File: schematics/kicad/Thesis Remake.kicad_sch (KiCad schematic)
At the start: 106 parts, among them J1 SJ2-35853B-SMT-TR, J2 Conn_01x18, J3 Conn_01x18, J4 Conn_01x01_Pin, J5 Conn_01x01_Pin, J6 Conn_01x01_Pin, J7 Conn_01x01_Pin, Q1 MMBT7002K, U10 MCP6001-OT, U11 MCP6001-OT, U2 PCM5102, U3 SN74LVC1G3157, U5 RT9080-33GJ5, U6 LM2940CT-5.0_MOD, U7 TPA711, U8 LM2940CT-5.0_MOD, U9 MCP6001-OT

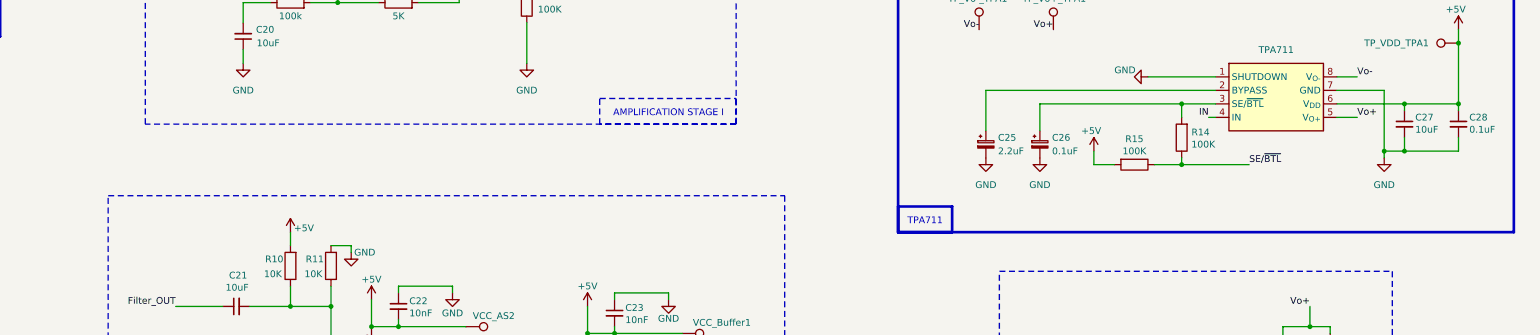
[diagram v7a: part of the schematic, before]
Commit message: Bluetooth works. Waveform generation works.
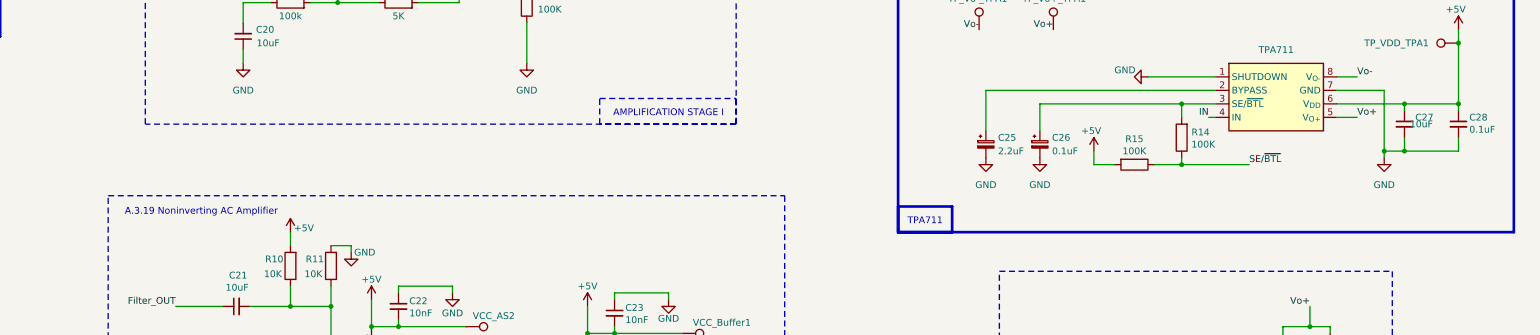
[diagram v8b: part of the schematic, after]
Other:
- note added: "A.3.19 Noninverting AC Amplifier"
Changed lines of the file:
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@@
 				(size 1.27 1.27)
 			)
+			(href "https://www.mouser.de/ProductDetail/Texas-Instruments/LM2940CT-5.0?qs=X1J7HmVL2ZHPtClZnI0H9A%3D%3D&srsltid=AfmBOooXmYCn6kktzCuK6TYLYlqacIcQRMEHhtZtGWFUuRpZVCvzZQb-")
 		)
 	)
@@
 				(size 1.27 1.27)
 			)
+			(href "https://www.mouser.de/ProductDetail/Texas-Instruments/LM2940CT-5.0?qs=X1J7HmVL2ZHPtClZnI0H9A%3D%3D&srsltid=AfmBOooXmYCn6kktzCuK6TYLYlqacIcQRMEHhtZtGWFUuRpZVCvzZQb-")
 		)
 	)
@@
 		)
 	)
+	(text "A.3.19 Noninverting AC Amplifier"
+		(exclude_from_sim no)
+		(at 309.626 120.65 0)
+		(effects
+			(font
+				(size 1.27 1.27)
+			)
+		)
+	)
 	(text "JACK OUTPUT"
 		(exclude_from_sim no)
@@
 				(size 1.27 1.27)
 			)
+			(href "https://www.mouser.de/ProductDetail/Richtek/RT9080-33GJ5?qs=amGC7iS6iy9hJG6yuLjyPQ%3D%3D")
 		)
 	)
@@
 			"AAAAAAAAAAAAAAAAAAAAAAAAAAAAAAAAAAAAAAAAAAAAAAAAAAAAAAAAAAAAAAAAAAAAAAAAAAAA"
 			"AAAAAAAAAAAAAAAAAAAAAAAAAAAAAAAAAAAAAAAAAAAAAAAAAAAAAAAAAAAAAAAAAAAAAAAAAAAA"
+			"AAAAAAAAAAAAAAAAAAAAAAAAAAAAAAAAAAAAAAAAAAAAAAAAAAAAAAAAAAAAAAAAAAAAAAAAAAAA"
+			"AAAAAAAAAAAAAAAAAAAAAAAAAAAAAAAAAAAAAAAAAAAAAAAAAAAAAAAAAAAAAAAAAAAAAAAAAAAA"
+			"AAAAAAAAAAAAAAAAAAAAAAAAAAAAAAAAAAAAAAAAAAAAAAAAAAAAAAAAAAAAAAAAAAAAAAAAAAAA"
+			"AAAAAAAAAAAAAAAAAAAAAAAAAAAAAAAAAAAAAAAAAAAAAAAAAAAAAAAAAAAAAAAAAAAAAAAAAAAA"
+			"AAAAAAAAAAAAAAAAAAAAAAAAAAAAAAAAAAAAAAAAAAAAAAAAAAAAAAAAAAAAAAAAAAAAAAAAAAAA"
+			"AAAAAAAAAAAAAAAAAAAAAAAAAAAAAAAAAAAAAAAAAAAAAAAAAAAAAAAAAAAAAAAAAAAAAAAAAAAA"
+			"AAAAAAAAAAAAAAAAAAAAAAAAAAAAAAAAAAAAAAAAAAAAAAAAAAAAAAAAAAAAAAAAAAAAAAAAAAAA"
+			"AAAAAAAAAAAAAAAAAAAAAAAAAAAAAAAAAAAAAAAAAAAAAAAAAAAAAAAAAAAAAAAAAAAAAAAAAAAA"
+			"AAAAAAAAAAAAAAAAAAAAAAAAAAAAAAAAAAAAAAAAAAAAAAAAAAAAAAAAAAAAAAAAAAAAAAAAAAAA"
+			"AAAAAAAAAAAAAAAAAAAAAAAAAAAAAAAAAAAAAAAAAAAAAAAAAAAAAAAAAAAAAAAAAAAAAAAAAAAA"
+			"AAAAAAAAAAAAAAAAAAAAAAAAAAAAAAAAAAAAAAAAAAAAAAAAAAAAAAAAAAAAAAAAAAAAAAAAAAAA"
+			"AAAAAAAAAAAAAAAAAAAAAAAAAAAAAAAAAAAAAAAAAAAAAAAAAAAAAAAAAAAAAAAAAAAAAAAAAAAA"
+			"AAAAAAAAAAAAAAAAAAAAAAAAAAAAAAAAAAAAAAAAAAAAAAAAAAAAAAAAAAAAAAAAAAAAAAAAAAAA"
+			"AAAAAAAAAAAAAAAAAAAAAAAAAAAAAAAAAAAAAAAAAAAAAAAAAAAAAAAAAAAAAAAAAAAAAAAAAAAA"
+			"AAAAAAAAAAAAAAAAAAAAAAAAAAAAAAAAAAAAAAAAAAAAAAAAAAAAAAAAAAAAAAAAAAAAAAAAAAAA"
+			"AAAAAAAAAAAAAAAAAAAAAAAAAAAAAAAAAAAAAAAAAAAAAAAAAAAAAAAAAAAAAAAAAAAAAAAAAAAA"
+			"AAAAAAAAAAAAAAAAAAAAAAAAAAAAAAAAAAAAAAAAAAAAAAAAAAAAAAAAAAAAAAAAAAAAAAAAAAAA"
+			"AAAAAAAAAAAAAAAAAAAAAAAAAAAAAAAAAAAAAAAAAAAAAAAAAAAAAAAAAAAAAAAAAAAAAAAAAAAA"
+			"AAAAAAAAAAAAAAAAAAAAAAAAAAAAAAAAAAAAAAAAAAAAAAAAAAAAAAAAAAAAAAAAAAAAAAAAAAAA"
+			"AAAAAAAAAAAAAAAAAAAAAAAAAAAAAAAAAAAAAAAAAAAAAAAAAAAAAAAAAAAAAAAAAAAAAAAAAAAA"
+			"AAAAAAAAAAAAAAAAAAAAAAAAAAAAAAAAAAAAAAAAAAAAAAAAAAAAAAAAAAAAAAAAAAAAAAAAAAAA"
+			"AAAAAAAAAAAAAAAAAAAAAAAAAAAAAAAAAAAAAAAAAAAAAAAAAAAAAAAAAAAAAAAAAAAAAAAAAAAA"
+			"AAAAAAAAAAAAAAAAAAAAAAAAAAAAAAAAAAAAAAAAAAAAAAAAAAAAAAAAAAAAAAAAAAAAAAAAAAAA"
+			"AAAAAAAAAAAAAAAAAAAAAAAAAAAAAAAAAAAAAAAAAAAAAAAAAAAAAAAAAAAAAAAAAAAAAAAAAAAA"
+			"AAAAAAAAAAAAAAAAAAAAAAAAAAAAAAAAAAAAAAAAAAAAAAAAAAAAAAAAAAAAAAAAAAAAAAAAAAAA"
+			"AAAAAAAAAAAAAAAAAAAAAAAAAAAAAAAAAAAAAAAAAAAAAAAAAAAAAAAAAAAAAAAAAAAAAAAAAAAA"
+			"AAAAAAAAAAAAAAAAAAAAAAAAAAAAAAAAAAAAAAAAAAAAAAAAAAAAAAAAAAAAAAAAAAAAAAAAAAAA"
+			"AAAAAAAAAAAAAAAAAAAAAAAAAAAAAAAAAAAAAAAAAAAAAAAAAAAAAAAAAAAAAAAAAAAAAAAAAAAA"
+			"AAAAAAAAAAAAAAAAAAAAAAAAAAAAAAAAAAAAAAAAAAAAAAAAAAAAAAAAAAAAAAAAAAAAAAAAAAAA"
+			"AAAAAAAAAAAAAAAAAAAAAAAAAAAAAAAAAAAAAAAAAAAAAAAAAAAAAAAAAAAAAAAAAAAAAAAAAAAA"
+			"AAAAAAAAAAAAAAAAAAAAAAAAAAAAAAAAAAAAAAAAAAAAAAAAAAAAAAAAAAAAAAAAAAAAAAAAAAAA"
+			"AAAAAAAAAAAAAAAAAAAAAAAAAAAAAAAAAAAAAAAAAAAAAAAAAAAAAAAAAAAAAAAAAAAAAAAAAAAA"
+			"AAAAAAAAAAAAAAAAAAAAAAAAAAAAAAAAAAAAAAAAAAAAAAAAAAAAAAAAAAAAAAAAAAAAAAAAAAAA"
+			"AAAAAAAAAAAAAAAAAAAAAAAAAAAAAAAAAAAAAAAAAAAAAAAAAAAAAAAAAAAAAAAAAAAAAAAAAAAA"
+			"AAAAAAAAAAAAAAAAAAAAAAAAAAAAAAAAAAAAAAAAAAAAAAAAAAAAAAAAAAAAAAAAAAAAAAAAAAAA"
+			"AAAAAAAAAAAAAAAAAAAAAAAAAAAAAAAAAAAAAAAAAAAAAAAAAAAAAAAAAAAAAAAAAAAAAAAAAAAA"
+			"AAAAAAAAAAAAAAAAAAAAAAAAAAAAAAAAAAAAAAAAAAAAAAAAAAAAAAAAAAAAAAAAAAAAAAAAAAAA"
+			"AAAAAAAAAAAAAAAAAAAAAAAAAAAAAAAAAAAAAAAAAAAAAAAAAAAAAAAAAAAAAAAAAAAAAAAAAAAA"
+			"AAAAAAAAAAAAAAAAAAAAAAAAAAAAAAAAAAAAAAAAAAAAAAAAAAAAAAAAAAAAAAAAAAAAAAAAAAAA"
+			"AAAAAAAAAAAAAAAAAAAAAAAAAAAAAAAAAAAAAAAAAAAAAAAAAAAAAAAAAAAAAAAAAAAAAAAAAAAA"
+			"AAAAAAAAAAAAAAAAAAAAAAAAAAAAAAAAAAAAAAAAAAAAAAAAAAAAAAAAAAAAAAAAAAAAAAAAAAAA"
+			"AAAAAAAAAAAAAAAAAAAAAAAAAAAAAAAAAAAAAAAAAAAAAAAAAAAAAAAAAAAAAAAAAAAAAAAAAAAA"
+			"AAAAAAAAAAAAAAAAAAAAAAAAAAAAAAAAAAAAAAAAAAAAAAAAAAAAAAAAAAAAAAAAAAAAAAAAAAAA"
+			"AAAAAAAAAAAAAAAAAAAAAAAAAAAAAAAAAAAAAAAAAAAAAAAAAAAAAAAAAAAAAAAAAAAAAAAAAAAA"
+			"AAAAAAAAAAAAAAAAAAAAAAAAAAAAAAAAAAAAAAAAAAAAAAAAAAAAAAAAAAAAAAAAAAAAAAAAAAAA"
+			"AAAAAAAAAAAAAAAAAAAAAAAAAAAAAAAAAAAAAAAAAAAAAAAAAAAAAAAAAAAAAAAAAAAAAAAAAAAA"
+			"AAAAAAAAAAAAAAAAAAAAAAAAAAAAAAAAAAAAAAAAAAAAAAAAAAAAAAAAAAAAAAAAAAAAAAAAAAAA"
+			"AAAAAAAAAAAAAAAAAAAAAAAAAAAAAAAAAAAAAAAAAAAAAAAAAAAAAAAAAAAAAAAAAAAAAAAAAAAA"
+			"AAAAAAAAAAAAAAAAAAAAAAAAAAAAAAAAAAAAAAAAAAAAAAAAAAAAAAAAAAAAAAAAAAAAAAAAAAAA"
+			"AAAAAAAAAAAAAAAAAAAAAAAAAAAAAAAAAAAAAAAAAAAAAAAAAAAAAAAAAAAAAAAAAAAAAAAAAAAA"
+			"AAAAAAAAAAAAAAAAAAAAAAAAAAAAAAAAAAAAAAAAAAAAAAAAAAAAAAAAAAAAAAAAAAAAAAAAAAAA"
+			"AAAAAAAAAAAAAAAAAAAAAAAAAAAAAAAAAAAAAAAAAAAAAAAAAAAAAAAAAAAAAAAAAAAAAAAAAAAA"
+			"AAAAAAAAAAAAAAAAAAAAAAAAAAAAAAAAAAAAAAAAAAAAAAAAAAAAAAAAAAAAAAAAAAAAAAAAAAAA"
+			"AAAAAAAAAAAAAAAAAAAAAAAAAAAAAAAAAAAAAAAAAAAAAAAAAAAAAAAAAAAAAAAAAAAAAAAAAAAA"
+			"AAAAAAAAAAAAAAAAAAAAAAAAAAAAAAAAAAAAAAAAAAAAAAAAAAAAAAAAAAAAAAAAAAAAAAAAAAAA"
+			"AAAAAAAAAAAAAAAAAAAAAAAAAAAAAAAAAAAAAAAAAAAAAAAAAAAAAAAAAAAAAAAAAAAAAAAAAAAA"
+			"AAAAAAAAAAAAAAAAAAAAAAAAAAAAAAAAAAAAAAAAAAAAAAAAAAAAAAAAAAAAAAAAAAAAAAAAAAAA"
+			"AAAAAAAAAAAAAAAAAAAAAAAAAAAAAAAAAAAAAAAAAAAAAAAAAAAAAAAAAAAAAAAAAAAAAAAAAAAA"
+			"AAAAAAAAAAAAAAAAAAAAAAAAAAAAAAAAAAAAAAAAAAAAAAAAAAAAAAAAAAAAAAAAAAAAAAAAAAAA"
+			"AAAAAAAAAAAAAAAAAAAAAAAAAAAAAAAAAAAAAAAAAAAAAAAAAAAAAAAAAAAAAAAAAAAAAAAAAAAA"
+			"AAAAAAAAAAAAAAAAAAAAAAAAAAAAAAAAAAAAAAAAAAAAAAAAAAAAAAAAAAAAAAAAAAAAAAAAAAAA"
+			"AAAAAAAAAAAAAAAAAAAAAAAAAAAAAAAAAAAAAAAAAAAAAAAAAAAAAAAAAAAAAAAAAAAAAAAAAAAA"
+			"AAAAAAAAAAAAAAAAAAAAAAAAAAAAAAAAAAAAAAAAAAAAAAAAAAAAAAAAAAAAAAAAAAAAAAAAAAAA"
+			"AAAAAAAAAAAAAAAAAAAAAAAAAAAAAAAAAAAAAAAAAAAAAAAAAAAAAAAAAAAAAAAAAAAAAAAAAAAA"
+			"AAAAAAAAAAAAAAAAAAAAAAAAAAAAAAAAAAAAAAAAAAAAAAAAAAAAAAAAAAAAAAAAAAAAAAAAAAAA"
+			"AAAAAAAAAAAAAAAAAAAAAAAAAAAAAAAAAAAAAAAAAAAAAAAAAAAAAAAAAAAAAAAAAAAAAAAAAAAA"
+			"AAAAAAAAAAAAAAAAAAAAAAAAAAAAAAAAAAAAAAAAAAAAAAAAAAAAAAAAAAAAAAAAAAAAAAAAAAAA"
+			"AAAAAAAAAAAAAAAAAAAAAAAAAAAAAAAAAAAAAAAAAAAAAAAAAAAAAAAAAAAAAAAAAAAAAAAAAAAA"
+			"AAAAAAAAAAAAAAAAAAAAAAAAAAAAAAAAAAAAAAAAAAAAAAAAAAAAAAAAAAAAAAAAAAAAAAAAAAAA"
+			"AAAAAAAAAAAAAAAAAAAAAAAAAAAAAAAAAAAAAAAAAAAAAAAAAAAAAAAAAAAAAAAAAAAAAAAAAAAA"
+			"AAAAAAAAAAAAAAAAAAAAAAAAAAAAAAAAAAAAAAAAAAAAAAAAAAAAAAAAAAAAAAAAAAAAAAAAAAAA"
+			"AAAAAAAAAAAAAAAAAAAAAAAAAAAAAAAAAAAAAAAAAAAAAAAAAAAAAAAAAAAAAAAAAAAAAAAAAAAA"
+			"AAAAAAAAAAAAAAAAAAAAAAAAAAAAAAAAAAAAAAAAAAAAAAAAAAAAAAAAAAAAAAAAAAAAAAAAAAAA"
+			"AAAAAAAAAAAAAAAAAAAAAAAAAAAAAAAAAAAAAAAAAAAAAAAAAAAAAAAAAAAAAAAAAAAAAAAAAAAA"
+			"AAAAAAAAAAAAAAAAAAAAAAAAAAAAAAAAAAAAAAAAAAAAAAAAAAAAAAAAAAAAAAAAAAAAAAAAAAAA"
+			"AAAAAAAAAAAAAAAAAAAAAAAAAAAAAAAAAAAAAAAAAAAAAAAAAAAAAAAAAAAAAAAAAAAAAAAAAAAA"
+			"AAAAAAAAAAAAAAAAAAAAAAAAAAAAAAAAAAAAAAAAAAAAAAAAAAAAAAAAAAAAAAAAAAAAAAAAAAAA"
+			"AAAAAAAAAAAAAAAAAAAAAAAAAAAAAAAAAAAAAAAAAAAAAAAAAAAAAAAAAAAAAAAAAAAAAAAAAAAA"
+			"AAAAAAAAAAAAAAAAAAAAAAAAAAAAAAAAAAAAAAAAAAAAAAAAAAAAAAAAAAAAAAAAAAAAAAAAAAAA"
+			"AAAAAAAAAAAAAAAAAAAAAAAAAAAAAAAAAAAAAAAAAAAAAAAAAAAAAAAAAAAAAAAAAAAAAAAAAAAA"
+			"AAAAAAAAAAAAAAAAAAAAAAAAAAAAAAAAAAAAAAAAAAAAAAAAAAAAAAAAAAAAAAAAAAAAAAAAAAAA"
+			"AAAAAAAAAAAAAAAAAAAAAAAAAAAAAAAAAAAAAAAAAAAAAAAAAAAAAAAAAAAAAAAAAAAAAAAAAAAA"
+			"AAAAAAAAAAAAAAAAAAAAAAAAAAAAAAAAAAAAAAAAAAAAAAAAAAAAAAAAAAAAAAAAAAAAAAAAAAAA"
+			"AAAAAAAAAAAAAAAAAAAAAAAAAAAAAAAAAAAAAAAAAAAAAAAAAAAAAAAAAAAAAAAAAAAAAAAAAAAA"
+			"AAAAAAAAAAAAAAAAAAAAAAAAAAAAAAAAAAAAAAAAAAAAAAAAAAAAAAAAAAAAAAAAAAAAAAAAAAAA"
+			"AAAAAAAAAAAAAAAAAAAAAAAAAAAAAAAAAAAAAAAAAAAAAAAAAAAAAAAAAAAAAAAAAAAAAAAAAAAA"
+			"AAAAAAAAAAAAAAAAAAAAAAAAAAAAAAAAAAAAAAAAAAAAAAAAAAAAAAAAAAAAAAAAAAAAAAAAAAAA"
+			"AAAAAAAAAAAAAAAAAAAAAAAAAAAAAAAAAAAAAAAAAAAAAAAAAAAAAAAAAAAAAAAAAAAAAAAAAAAA"
+			"AAAAAAAAAAAAAAAAAAAAAAAAAAAAAAAAAAAAAAAAAAAAAAAAAAAAAAAAAAAAAAAAAAAAAAAAAAAA"
+			"AAAAAAAAAAAAAAAAAAAAAAAAAAAAAAAAAAAAAAAAAAAAAAAAAAAAAAAAAAAAAAAAAAAAAAAAAAAA"
 			"AAAAAAAAAAAAAAAAAAAAAAAAAAAAAAAAAA=="
 		)
@@
 		)
 		(property "Value" "10uF"
-			(at 537.972 105.156 0)
+			(at 536.956 104.14 0)
 			(effects
 				(font
